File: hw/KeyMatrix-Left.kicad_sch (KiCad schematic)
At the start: 127 parts, among them SW3300 SW_Cherry_MX_RGB, SW3301 SW_Cherry_MX_RGB, SW3302 SW_Cherry_MX_RGB, SW3303 SW_Cherry_MX_RGB, SW3304 SW_Cherry_MX_RGB, SW3305 SW_Cherry_MX_RGB, SW3306 SW_Cherry_MX_RGB, SW3307 SW_Cherry_MX_RGB, SW3308 SW_Cherry_MX_RGB, SW3309 SW_Cherry_MX_RGB, SW3310 SW_Cherry_MX_RGB, SW3311 SW_Cherry_MX_RGB, SW3312 SW_Cherry_MX_RGB, SW3313 SW_Cherry_MX_RGB, SW3314 SW_Cherry_MX_RGB, SW3315 SW_Cherry_MX_RGB, SW3316 SW_Cherry_MX_RGB, SW3317 SW_Cherry_MX_RGB, SW3318 SW_Cherry_MX_RGB, SW3319 SW_Cherry_MX_RGB, SW3320 SW_Cherry_MX_RGB, SW3321 SW_Cherry_MX_RGB, SW3322 SW_Cherry_MX_RGB, SW3323 SW_Cherry_MX_RGB, SW3324 SW_Cherry_MX_RGB, SW3325 SW_Cherry_MX_RGB, SW3326 SW_Cherry_MX_RGB, SW3327 SW_Cherry_MX_RGB, SW3328 SW_Cherry_MX_RGB, SW3329 SW_Cherry_MX_RGB, SW3330 SW_Cherry_MX_RGB, SW3331 SW_Cherry_MX_RGB, SW3332 SW_Cherry_MX_RGB, SW3333 SW_Cherry_MX_RGB, SW3334 SW_Cherry_MX_RGB, SW3335 SW_Cherry_MX_RGB, SW3336 SW_Cherry_MX_RGB, SW3337 SW_Cherry_MX_RGB, X3300 Keycap-R1-1x1, X3301 Keycap-R1-1x1, X3302 Keycap-R1-1x1, X3303 Keycap-R1-1x1, X3304 Keycap-R1-1x1, X3305 Keycap-R1-1x1, X3306 Keycap-R1-1x1, X3307 Keycap-R1-1x1, X3308 Keycap-R1-1x1, X3309 Keycap-R1-1x1, X3310 Keycap-R1-1x1, X3311 Keycap-R1-1x1, X3312 Keycap-R1-1x1, X3313 Keycap-R1-1.5x1, X3314 Keycap-R1-1x1, X3315 Keycap-R1-1x1, X3316 Keycap-R1-1x1, X3317 Keycap-R1-1x1, X3318 Keycap-R1-1x1, X3319 Keycap-R1-1.75x1, X3320 Keycap-R1-1x1, X3321 Keycap-R1-1x1, X3322 Keycap-R1-1x1, X3323 Keycap-R1-1x1, X3324 Keycap-R1-1x1, X3325 Keycap-R1-2x1, X3326 Keycap-R1-1.25x1, X3327 Keycap-R1-1x1, X3328 Keycap-R1-1x1, X3329 Keycap-R1-1x1, X3330 Keycap-R1-1x1, X3331 Keycap-R1-1x1, X3332 Keycap-R1-1.25x1, X3333 Keycap-R1-1.25x1, X3334 Keycap-R1-1.25x1, X3335 Keycap-R1-2.75x1, X3336 Keycap-R1-1x1, X3337 Keycap-R1-1x1, X3338 STAB-0G990224, X3339 STAB-0G990224

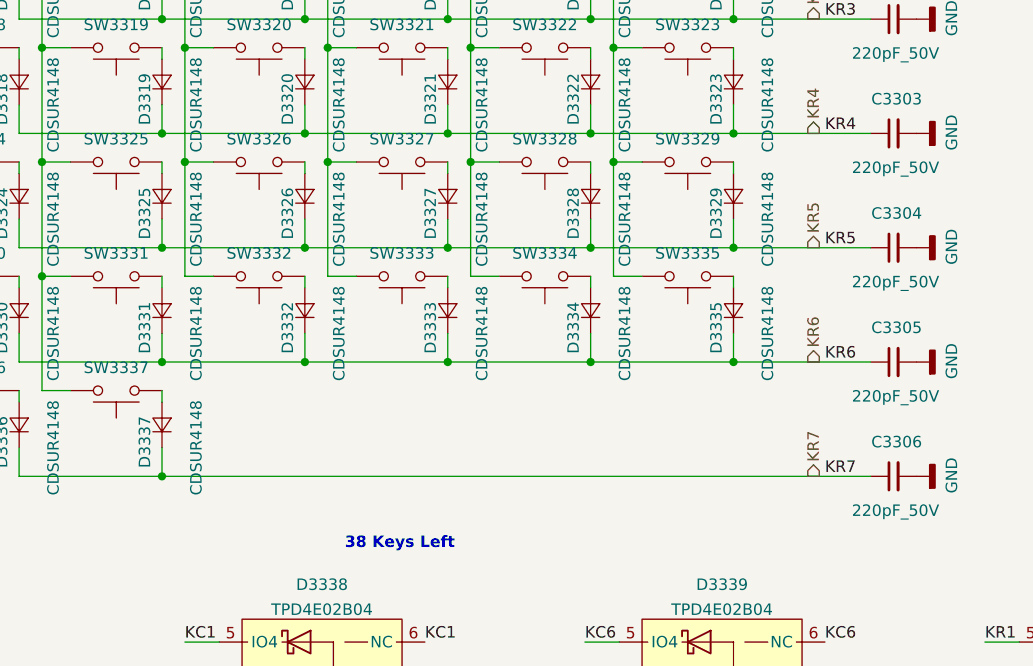
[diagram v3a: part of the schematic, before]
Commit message: Layout south facing keyboard PCB.
Furthermore, optimize matrix component placement foir cleaner layout.
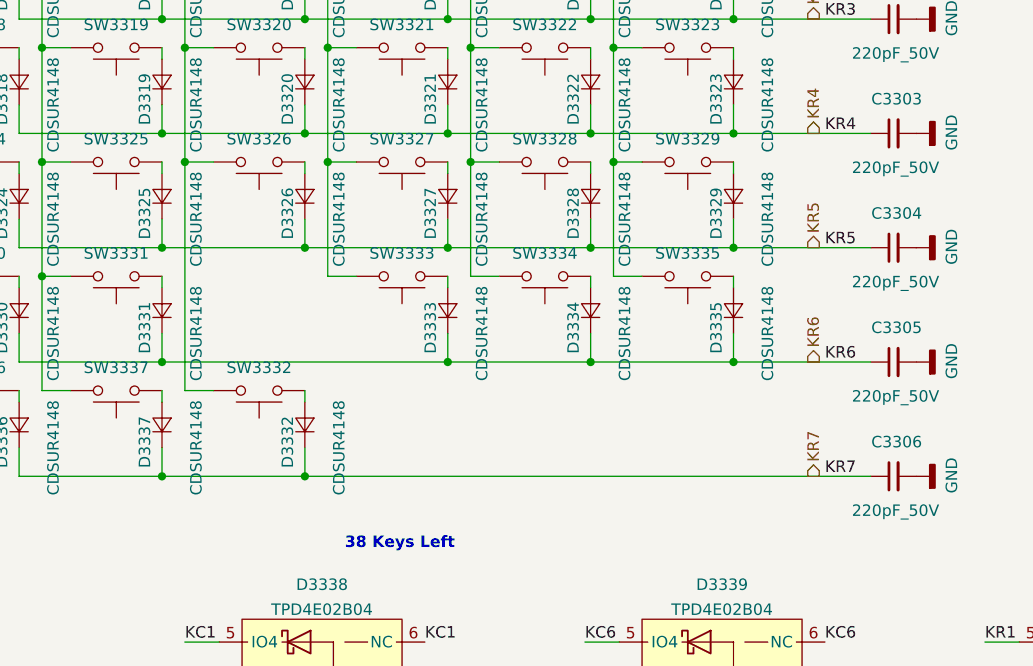
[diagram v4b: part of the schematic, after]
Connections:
- net KR6: no longer D3332.1 (K)
- net KR7: now also D3332.1 (K)
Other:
- moved on the sheet: D3332, SW3332
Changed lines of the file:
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@@
   (junction (at 25.4 38.1) (diameter 0) (color 0 0 0 0)
   )
+  (junction (at 70.485 111.125) (diameter 0) (color 0 0 0 0)
+  )
   (junction (at 73.025 63.5) (diameter 0) (color 0 0 0 0)
   )
@@
   )
   (junction (at 86.36 98.425) (diameter 0) (color 0 0 0 0)
-  )
-  (junction (at 70.485 98.425) (diameter 0) (color 0 0 0 0)
   )
   (junction (at 25.4 88.9) (diameter 0) (color 0 0 0 0)
@@
     (stroke (width 0) (type default) (color 0 0 0 0))
   )
+  (wire (pts (xy 70.485 111.125) (xy 133.35 111.125))
+    (stroke (width 0) (type default) (color 0 0 0 0))
+  )
   (wire (pts (xy 86.36 26.67) (xy 86.36 25.4))
     (stroke (width 0) (type default) (color 0 0 0 0))
@@
     (stroke (width 0) (type default) (color 0 0 0 0))
   )
+  (wire (pts (xy 70.485 101.6) (xy 70.485 102.87))
+    (stroke (width 0) (type default) (color 0 0 0 0))
+  )
   (wire (pts (xy 73.66 149.86) (xy 74.93 149.86))
     (stroke (width 0) (type default) (color 0 0 0 0))
@@
     (stroke (width 0) (type default) (color 0 0 0 0))
   )
-  (wire (pts (xy 70.485 95.25) (xy 70.485 98.425))
-    (stroke (width 0) (type default) (color 0 0 0 0))
-  )
   (wire (pts (xy 118.11 98.425) (xy 102.235 98.425))
     (stroke (width 0) (type default) (color 0 0 0 0))
@@
     (stroke (width 0) (type default) (color 0 0 0 0))
   )
-  (wire (pts (xy 54.61 111.125) (xy 133.35 111.125))
+  (wire (pts (xy 54.61 111.125) (xy 70.485 111.125))
     (stroke (width 0) (type default) (color 0 0 0 0))
   )
@@
     (stroke (width 0) (type default) (color 0 0 0 0))
   )
-  (wire (pts (xy 86.36 98.425) (xy 70.485 98.425))
-    (stroke (width 0) (type default) (color 0 0 0 0))
-  )
   (wire (pts (xy 38.735 44.45) (xy 38.735 47.625))
     (stroke (width 0) (type default) (color 0 0 0 0))
   )
+  (wire (pts (xy 70.485 107.95) (xy 70.485 111.125))
+    (stroke (width 0) (type default) (color 0 0 0 0))
+  )
   (wire (pts (xy 101.6 134.62) (xy 105.41 134.62))
     (stroke (width 0) (type default) (color 0 0 0 0))
@@
     (stroke (width 0) (type default) (color 0 0 0 0))
   )
+  (wire (pts (xy 57.15 101.6) (xy 60.325 101.6))
+    (stroke (width 0) (type default) (color 0 0 0 0))
+  )
   (wire (pts (xy 118.11 95.25) (xy 118.11 98.425))
     (stroke (width 0) (type default) (color 0 0 0 0))
@@
     (stroke (width 0) (type default) (color 0 0 0 0))
   )
-  (wire (pts (xy 57.15 88.9) (xy 60.325 88.9))
-    (stroke (width 0) (type default) (color 0 0 0 0))
-  )
   (wire (pts (xy 92.075 63.5) (xy 88.9 63.5))
     (stroke (width 0) (type default) (color 0 0 0 0))
@@
     (stroke (width 0) (type default) (color 0 0 0 0))
   )
-  (wire (pts (xy 70.485 90.17) (xy 70.485 88.9))
-    (stroke (width 0) (type default) (color 0 0 0 0))
-  )
   (wire (pts (xy 38.735 39.37) (xy 38.735 38.1))
     (stroke (width 0) (type default) (color 0 0 0 0))
   )
-  (wire (pts (xy 57.15 76.2) (xy 57.15 88.9))
+  (wire (pts (xy 57.15 76.2) (xy 57.15 101.6))
     (stroke (width 0) (type default) (color 0 0 0 0))
   )
@@
     (stroke (width 0) (type default) (color 0 0 0 0))
   )
-  (wire (pts (xy 70.485 98.425) (xy 54.61 98.425))
+  (wire (pts (xy 54.61 98.425) (xy 86.36 98.425))
     (stroke (width 0) (type default) (color 0 0 0 0))
   )
@@
     (pin "2")
   )
-  (symbol (lib_id "Keyboard:CDSUR4148") (at 70.485 92.71 90) (unit 1)
-    (in_bom yes) (on_board yes)
-    (property "Reference" "D3332" (id 0) (at 68.58 94.615 0))
-    (property "Value" "CDSUR4148" (id 1) (at 74.295 95.25 0))
-    (property "Footprint" "Keyboard:SOD-523" (id 2) (at 70.993 96.52 0)
-      (effects (font (size 1.27 1.27)) hide)
-    )
-    (property "Datasheet" "750-CDSUR4148" (id 3) (at 68.453 93.98 0)
-      (effects (font (size 1.27 1.27)) hide)
-    )
-    (property "mouser#" "750-CDSUR4148" (id 4) (at 65.913 91.44 0)
+  (symbol (lib_id "Keyboard:CDSUR4148") (at 70.485 105.41 90) (unit 1)
+    (in_bom yes) (on_board yes)
+    (property "Reference" "D3332" (id 0) (at 68.58 107.315 0))
+    (property "Value" "CDSUR4148" (id 1) (at 74.295 107.95 0))
+    (property "Footprint" "Keyboard:SOD-523" (id 2) (at 70.993 109.22 0)
+      (effects (font (size 1.27 1.27)) hide)
+    )
+    (property "Datasheet" "750-CDSUR4148" (id 3) (at 68.453 106.68 0)
+      (effects (font (size 1.27 1.27)) hide)
+    )
+    (property "mouser#" "750-CDSUR4148" (id 4) (at 65.913 104.14 0)
       (effects (font (size 1.524 1.524)) hide)
     )
@@
     (pin "2")
   )
-  (symbol (lib_id "Keyboard:SW_Cherry_MX_RGB") (at 65.405 88.9 0) (mirror x) (unit 1)
-    (in_bom yes) (on_board yes)
-    (property "Reference" "SW3332" (id 0) (at 65.405 86.36 0))
-    (property "Value" "SW_Cherry_MX_RGB" (id 1) (at 65.405 86.995 0)
-      (effects (font (size 1.27 1.27)) hide)
-    )
-    (property "Footprint" "Keyboard:SW_Cherry_MX1A_RGB" (id 2) (at 65.405 93.98 0)
-      (effects (font (size 1.27 1.27)) hide)
-    )
-    (property "Datasheet" "https://www.cherrymx.de/dev.html" (id 3) (at 65.405 93.98 0)
-      (effects (font (size 1.27 1.27)) hide)
-    )
-    (property "reichelt#" "CHERRY MX1A-G1NA" (id 4) (at 65.405 88.9 0)
-      (effects (font (size 1.27 1.27)) hide)
-    )
+  (symbol (lib_id "Keyboard:SW_Cherry_MX_RGB") (at 65.405 101.6 0) (mirror x) (unit 1)
+    (in_bom yes) (on_board yes)
+    (property "Reference" "SW3332" (id 0) (at 65.405 99.06 0))
+    (property "Value" "SW_Cherry_MX_RGB" (id 1) (at 65.405 99.695 0)
+      (effects (font (size 1.27 1.27)) hide)
+    )
+    (property "Footprint" "Keyboard:SW_Cherry_MX1A_RGB" (id 2) (at 65.405 106.68 0)
+      (effects (font (size 1.27 1.27)) hide)
+    )
+    (property "Datasheet" "https://www.cherrymx.de/dev.html" (id 3) (at 65.405 106.68 0)
+      (effects (font (size 1.27 1.27)) hide)
+    )
+    (property "reichelt#" "CHERRY MX1A-G1NA" (id 4) (at 65.405 101.6 0)
+      (effects (font (size 1.27 1.27)) hide)
+    )
